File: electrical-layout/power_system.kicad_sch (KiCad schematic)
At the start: 14 parts, among them Q1 Q_NMOS_Depletion, Q2 NMOS, Q3 NMOS, Q4 NMOS, Q5 NMOS, SW1 SW_Push

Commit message: layout-2025: update many parts of the layout
What a goooood commit message!

... sorry
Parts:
- removed F3: 70A, symbol Device:Fuse
- removed Q1: Q_NMOS_Depletion, symbol Device:Q_NMOS_Depletion
- removed Q2, Q3, Q4, Q5: NMOS, symbol Simulation_SPICE:NMOS
- removed SW1: SW_Push, symbol Switch:SW_Push
- removed U19: ~, symbol Exocet:Charge_Controller
- removed U3: ~, symbol Exocet:Protium-2500
- removed U4: ~, symbol Exocet:Power_Control_Pcb
- added F2: 50A, symbol Device:Fuse
- added F4: 120A, symbol Device:Fuse
- added F5: 30A, symbol Device:Fuse
- added J2: HV- Busbar, symbol Exocet:Busbar_6
- added J3: HV+ Busbar, symbol Exocet:Busbar_6
- added J4: Storage Battery Charge Connector, symbol Connector_Generic:Conn_01x02
- added J5: Auxiliary Battery Charge Connector, symbol Connector_Generic:Conn_01x02
- added K1: BOP Switch, symbol Relay:Relay_SPST-NO
- added K10, K4: DC-DC Precharge Stage 2, symbol Relay:Relay_SPST-NO
- added K11, K8: Brake Resistor Switch 1, symbol Relay:Relay_SPDT
- added K3: Storage Battery Switch, symbol Relay:Relay_SPST-NO
- added K5, K9: DC-DC Precharge Stage 1, symbol Relay:Relay_SPST-NO
- added K7: Auxiliary Battery Switch, symbol Relay:Relay_SPST-NO
- added R2, R5: 100, symbol Device:R
- added R3, R6: ?m, symbol Device:R
- added SW5: Motor Switch, symbol Switch:SW_Push
- added U18: Fuel Cell Controller, symbol Exocet:Protium_2500_Controller
- added U19: Insulation Monitoring Device, symbol Exocet:Insulation_Controller
- added U20: Fuel Cell, symbol Exocet:Protium_2500_Fuel_Cell
- added U21: MPPT Charge Controller, symbol Exocet:Charge_Controller
- added U22: Power Sensor, symbol Exocet:MEBC_Power_Sense
- added U3: Storage Battery, symbol Exocet:Storage_Battery
- BT2: value 48V (25Ah) -> Auxiliary Battery; MFG (none) -> Ionic; MPN (none) -> IC-48V25-EP; Manufacturer Ionic -> (none); Part IC-48V25-EP -> (none)
- F1: value ??A -> 300A; MFR (none) -> Rim Drive Technology
- R1: value 1.5 (2kW) -> Braking Resistor; DIST (none) -> Mouster; MFR (none) -> TE Connectivity; MPN (none) -> TE2000B1R5J; Manufacturer TE Connectivity -> (none); Part TE2000B1R5J -> (none)
- U1: value ~ -> Motor; MFR (none) -> Rim Drive Technology; MPN (none) -> Outboard 5.0; Manufacturer Rim Drive Technology -> (none); Part Outdrive 5.0 -> (none)
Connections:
- net at F1.2: now also U22.; no longer U1.1 (+)
- net at F1.1: now also K11.11, K8.11, SW5.2
- net at BT2.1 (+): now also J5.1 (Pin_1), K7.13
- net AUXILIARY_BATT-: now reaches BT2.2 (-)
- net AUXILIARY_BATT-: now also J2., J5.2 (Pin_2), U19. (BUS-)
- net BRAKE_CTRL_S: no longer names the net of R1.1
- net BRAKE_CTRL_S: now also J2.
- net GND: no longer names the net of R1.2
- net GND: now also K11.12, K8.12; no longer U1.2 (-)
- new net: K11.A1, K8.A1
- new net: K11.A2, K8.A2
- new net: K3.13, U3. (VCC)
- new net: J4.1 (Pin_1), U3. (VCC)
- new net: J4.2 (Pin_2), U3. (VCC)
- new net: K4.13, R2.2, U21. (L)
- new net: F2.1, U21. (L)
- new net: F4.2, J3., U19. (BUS-)
- new net: U1. (...), U22. (x2)
- new net: J2., U22.
- new net: J2., U18. (SIGNAL)
- new net: F5.1, U18. (SIGNAL)
- new net: U18. (SIGNAL), U20. (SIGNAL) (x5)
- new net: K10.13, R5.2, SW5.1
- new net: J3., K10.14, K9.14
- new net: K5.13, R2.1
- new net: K9.13, R5.1
- new net: F5.2, K4.14, K5.14
- new net: J3., K1.14
- new net AUXILIARY_SHUNT+: F2.2, F4.1, R6.1
- new net AUXILIARY_SHUNT-: K7.14, R6.2
- new net BOP+: K1.13, U18. (SIGNAL)
- new net CHARGE_CTLR_OUT-: J2., U21. (L)
- new net Frame: U19. (BUS-)
- new net HV_BUS+: J3.
- new net HV_BUS-: J2.
- new net STORAGE_BATT-: U21. (L), U3. (VCC)
- new net STORAGE_SHUNT+: R3.1, U18. (SIGNAL)
- new net STORAGE_SHUNT-: K3.14, R3.2
- no-connect marks 0 -> 15
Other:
- note added: "C-AN01"
- note added: "C-AN02"
- note added: "C-AP01"
- note added: "C-AP02"
- note added: "C-AP03"
- note added: "C-AP04"
- note added: "C-AP05"
- note added: "C-BN01"
- note added: "ZONE A"
- note added: "ZONE B"
- note added: "ZONE C"
- note removed: "Isolated from frame"

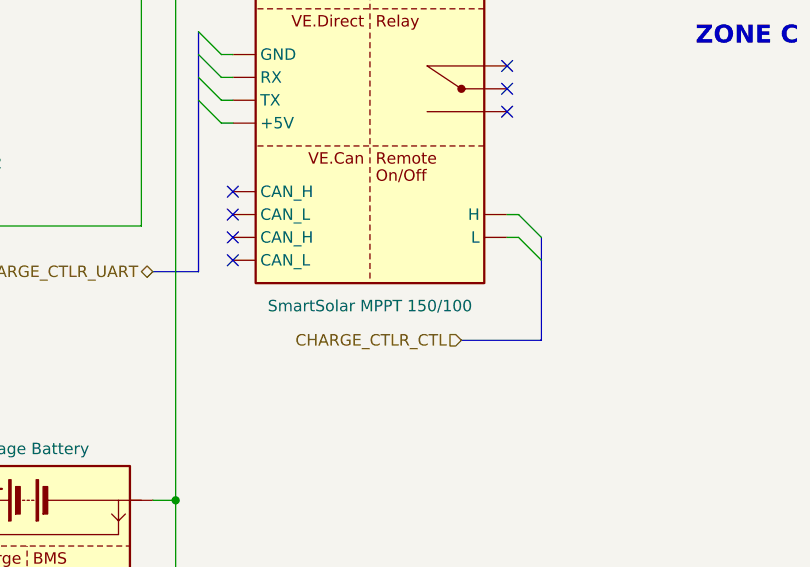
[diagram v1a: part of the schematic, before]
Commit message: layout-2025: add power breadboard and connections
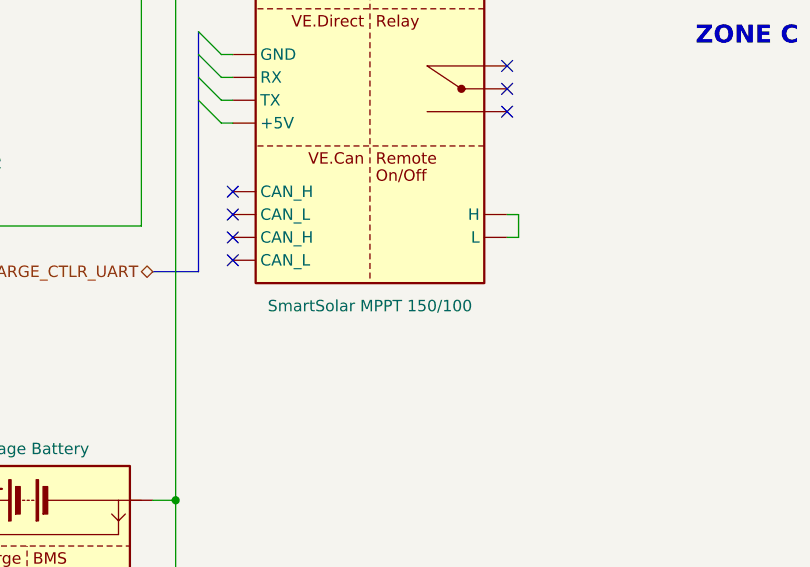
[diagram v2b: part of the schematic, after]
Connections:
- net at U22.: now also F1.2; no longer U1. (...)
- net at U1. (...): no longer U22.
- new net: F4.2, J3., U19. (BUS-)
- new net: U1. (...), U22. (x2)
- new net: J2., U22.
- new net: J2., U18. (SIGNAL)
- new net: U18. (SIGNAL), U20. (SIGNAL) (x4)
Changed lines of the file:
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@@
 	(title_block
 		(title "Power System")
-		(date "2026-05-15")
+		(date "2026-07-04")
 		(rev "1.1.0")
 	)
@@
 	)
 	(bus_entry
-		(at 250.19 53.34)
-		(size 2.54 2.54)
-		(stroke
-			(width 0)
-			(type default)
-		)
-	)
-	(bus_entry
 		(at 76.2 138.43)
 		(size 2.54 2.54)
@@
 	)
 	(bus_entry
-		(at 250.19 50.8)
-		(size 2.54 2.54)
-		(stroke
-			(width 0)
-			(type default)
-		)
-	)
-	(bus_entry
 		(at 105.41 100.33)
 		(size 2.54 2.54)
@@
 		)
 	)
+	(wire
+		(pts
+			(xy 250.19 53.34) (xy 248.92 53.34)
+		)
+		(stroke
+			(width 0)
+			(type default)
+		)
+	)
 	(bus
 		(pts
@@
 		)
 	)
+	(wire
+		(pts
+			(xy 250.19 50.8) (xy 250.19 53.34)
+		)
+		(stroke
+			(width 0)
+			(type default)
+		)
+	)
 	(bus
 		(pts
@@
 	(wire
 		(pts
-			(xy 248.92 50.8) (xy 250.19 50.8)
-		)
-		(stroke
-			(width 0)
-			(type default)
-		)
-	)
-	(wire
-		(pts
 			(xy 74.93 138.43) (xy 76.2 138.43)
 		)
@@
 		)
 	)
-	(bus
-		(pts
-			(xy 243.84 64.77) (xy 252.73 64.77)
-		)
-		(stroke
-			(width 0)
-			(type default)
-			(color 194 194 0 1)
-		)
-	)
 	(wire
 		(pts
@@
 	(wire
 		(pts
+			(xy 248.92 50.8) (xy 250.19 50.8)
+		)
+		(stroke
+			(width 0)
+			(type default)
+		)
+	)
+	(wire
+		(pts
 			(xy 107.95 105.41) (xy 107.95 111.76)
 		)
@@
 		)
 	)
-	(bus
-		(pts
-			(xy 252.73 55.88) (xy 252.73 64.77)
-		)
-		(stroke
-			(width 0)
-			(type default)
-			(color 194 194 0 1)
-		)
-	)
 	(wire
 		(pts
@@
 		)
 	)
-	(bus
-		(pts
-			(xy 252.73 53.34) (xy 252.73 55.88)
-		)
-		(stroke
-			(width 0)
-			(type default)
-			(color 194 194 0 1)
-		)
-	)
 	(wire
 		(pts
@@
 	(wire
 		(pts
-			(xy 248.92 53.34) (xy 250.19 53.34)
-		)
-		(stroke
-			(width 0)
-			(type default)
-		)
-	)
-	(wire
-		(pts
 			(xy 85.09 163.83) (xy 88.9 163.83)
 		)
@@
 		(effects
 			(font
-				(size 1.27 1.27)
-			)
-			(justify right)
-		)
-	)
-	(hierarchical_label "CHARGE_CTLR_CTL"
-		(shape input)
-		(at 243.84 64.77 180)
-		(effects
-			(font

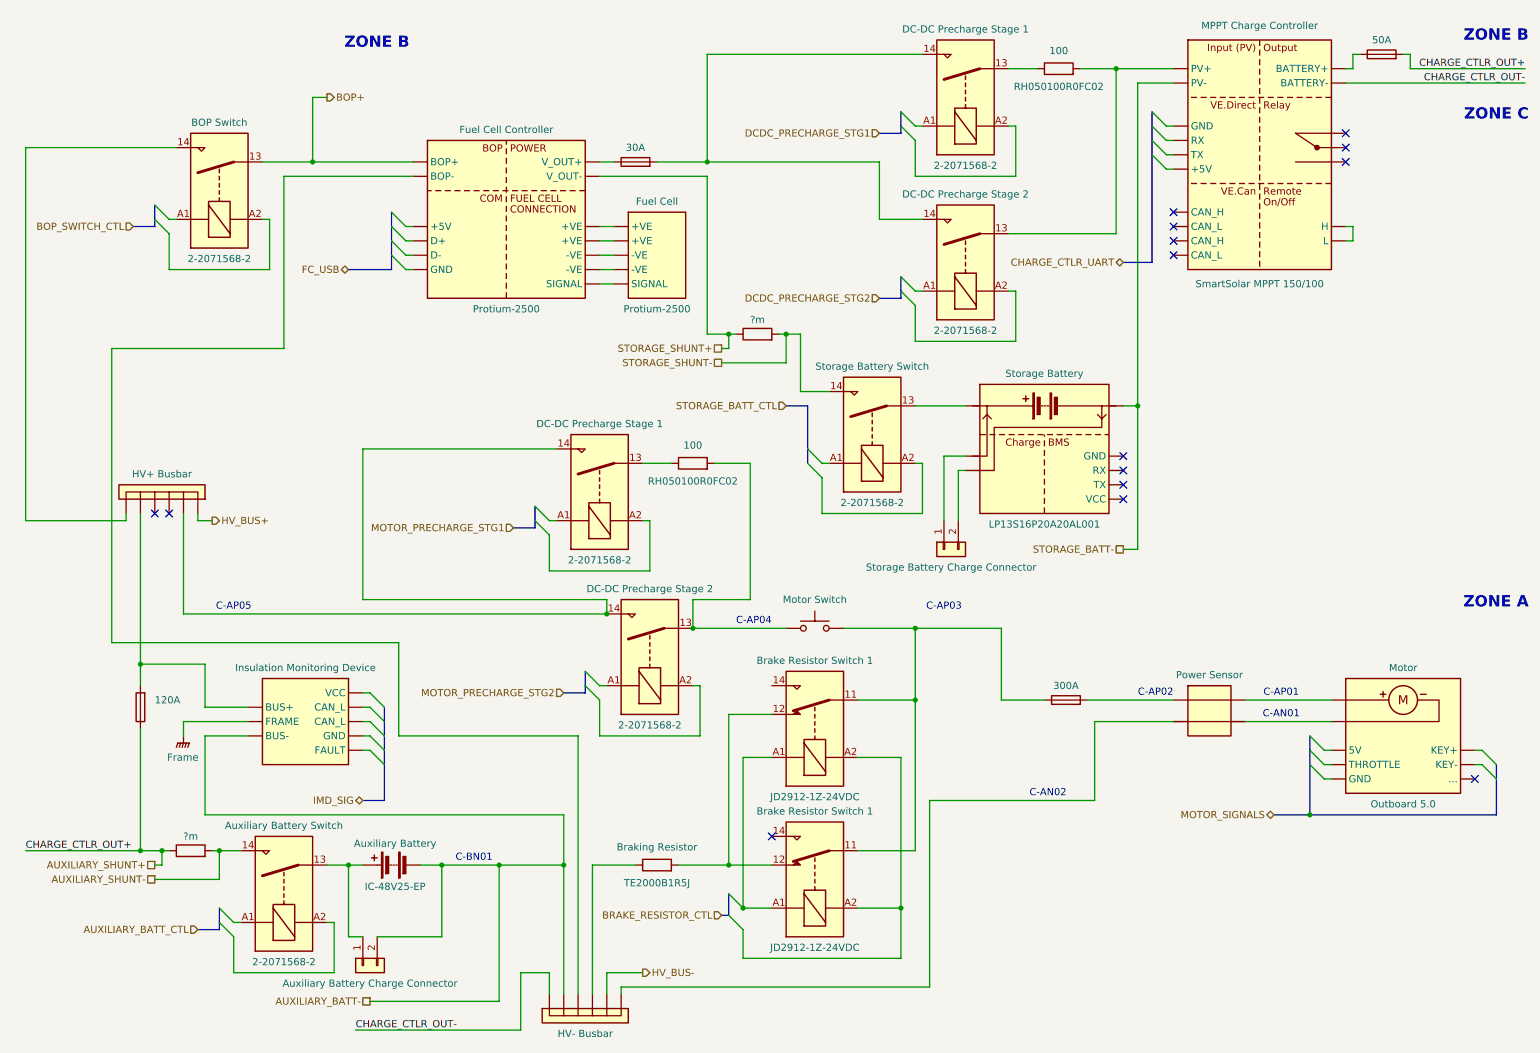
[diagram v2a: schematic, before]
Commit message: layout-2025: complete layout
- Added wire gauge from memory: must be checked once we get to the
  competition.
- Finalized all connections
- Moved a fuse
- Changed relay part number for some relays/contactors
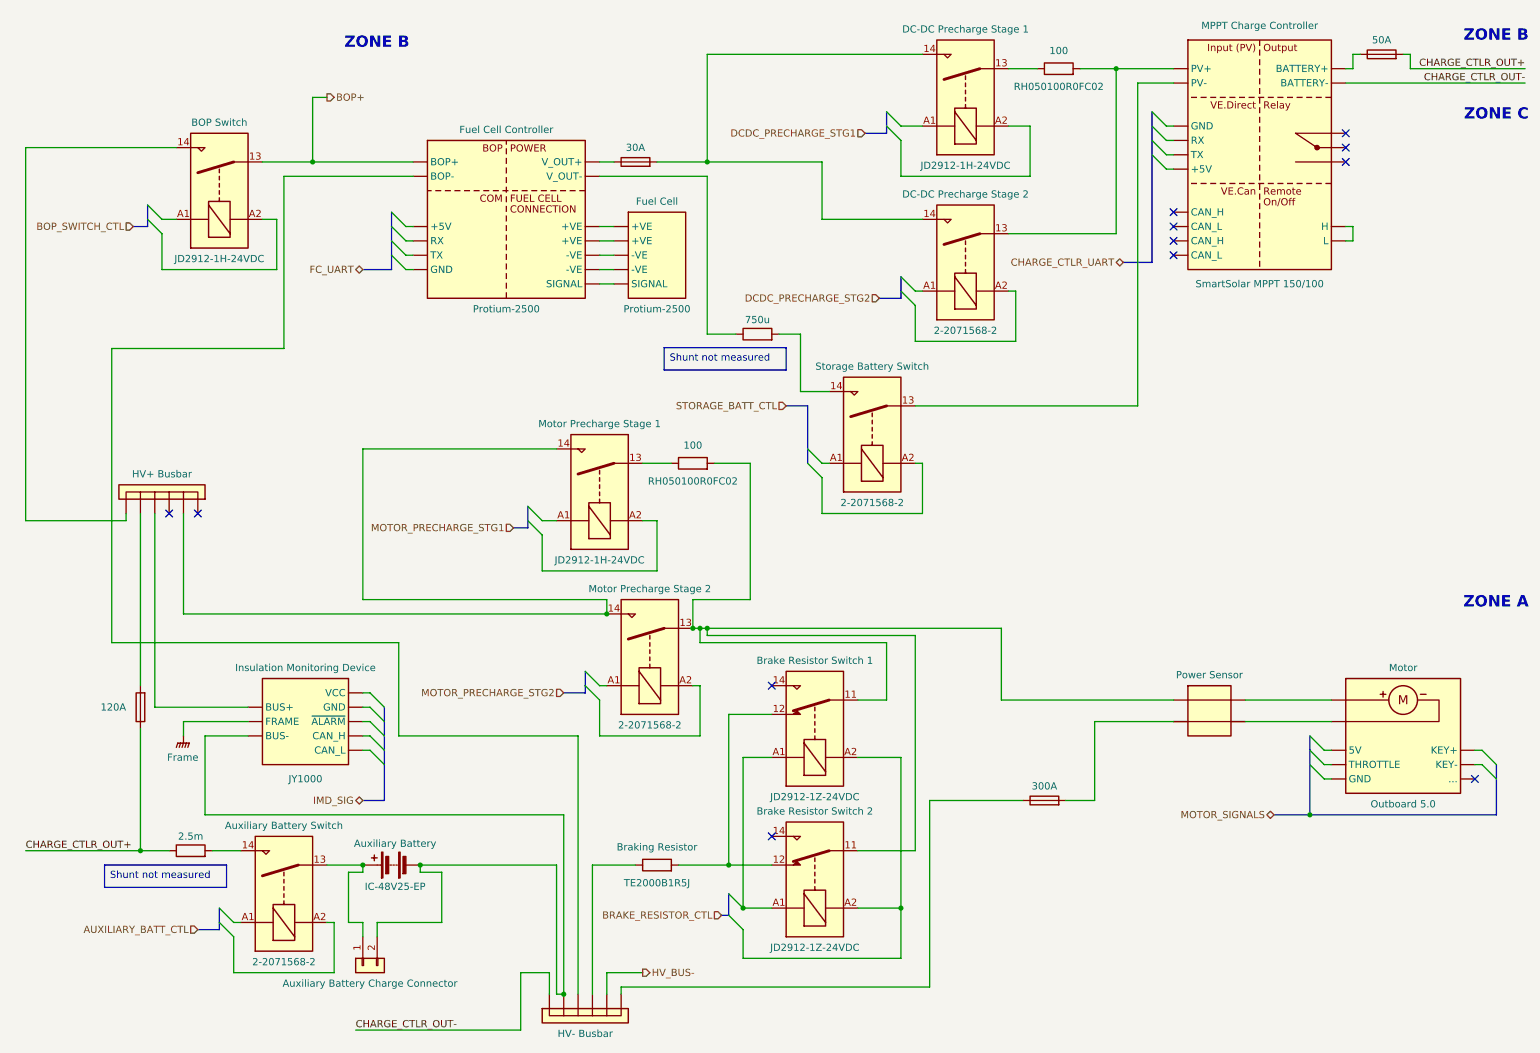
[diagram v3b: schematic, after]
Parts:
- removed J4: Storage Battery Charge Connector, symbol Connector_Generic:Conn_01x02
- removed SW5: Motor Switch, symbol Switch:SW_Push
- removed U3: Storage Battery, symbol Exocet:Storage_Battery
- K1, K5: MPN 2-2071568-2 -> JD2912-1H-24VDC
- K10: value DC-DC Precharge Stage 2 -> Motor Precharge Stage 2
- K8: value Brake Resistor Switch 1 -> Brake Resistor Switch 2
- K9: value DC-DC Precharge Stage 1 -> Motor Precharge Stage 1; MPN 2-2071568-2 -> JD2912-1H-24VDC
- R3: value ?m -> 750u
- R6: value ?m -> 2.5m
- U19: MPN (none) -> JY1000
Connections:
- net HV_BUS+ is gone; now on an unnamed net: J3.
- net STORAGE_BATT- is gone; now on net CHARGE_CTLR_OUT-: U21. (L)
- net at K11.11, K8.11: now also K10.13, R5.2, U22.; no longer F1.1
- net at K3.13: now also U21. (L)
- net at U22.: now also F1.2; no longer U1. (...)
- net at U1. (...): no longer U22.
- net at J3.: now also K1.14
- net AUXILIARY_BATT-: no longer names the net of BT2.2 (-), J2., J5.2 (Pin_2), U19. (BUS-)
- net AUXILIARY_SHUNT+ renamed CHARGE_CTLR_OUT+
- net AUXILIARY_SHUNT-: no longer names the net of K7.14, R6.2
- net STORAGE_SHUNT+: no longer names the net of R3.1, U18. (SIGNAL)
- net STORAGE_SHUNT-: no longer names the net of K3.14, R3.2
- new net: F4.2, J3.
- new net: U1. (...), U22. (x2)
- new net: J2., U18. (SIGNAL)
- new net: U18. (SIGNAL), U20. (SIGNAL) (x4)
- new net: J3., U19. (BUS-)
- new net: F1.1, J2.
- no-connect marks 15 -> 12
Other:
- note removed: "C-AN01"
- note removed: "C-AN02"
- note removed: "C-AP01"
- note removed: "C-AP02"
- note removed: "C-AP03"
- note removed: "C-AP04"
- note removed: "C-AP05"
- note removed: "C-BN01"
